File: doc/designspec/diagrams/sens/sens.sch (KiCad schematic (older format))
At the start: 7 parts

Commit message: sensormodul schema, spi, led display, filters är på g
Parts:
- removed U?: ATmega1284-PU, Package_DIP:DIP-40_W15.24mm, symbol _NONAME_
- added U?: ADG419BN, Package_DIP:DIP-8_W7.62mm, symbol Analog_Switch:ADG419BN
- added _?: JMA162A, Display_7Segment:DA04-11SYKWA, symbol jma162a:JMA162A
- HALLEFFECTSENSOR: symbol hall-effect:A112X -> sens-rescue:A112X-hall-effect
- KRISTALLOSCILLATOR: symbol exo3:IQEXO-3 -> sens-rescue:IQEXO-3-exo3
- U?: symbol MCU_Microchip_ATmega:ATmega1284-PU -> sens-rescue:ATmega1284-PU-MCU_Microchip_ATmega
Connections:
- net labels added: MISO, MOSI, SPI_SCK, SS_Slave_Select
- wire segments 39 -> 76
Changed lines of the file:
@@
 $EndComp
-Wire Wire Line
-	6200 4350 8850 4350
 Wire Wire Line
 	8600 1450 6200 1450
@@
 Wire Wire Line
 	8250 1650 6200 1650
-Wire Wire Line
-	8200 5850 8200 4500
-Wire Wire Line
-	8200 4500 8850 4500
-Connection ~ 8200 4500
 Wire Wire Line
 	8200 2650 8800 2650
@@
 Connection ~ 8450 2050
 Wire Wire Line
-	8450 4650 8850 4650
-Wire Wire Line
 	5700 1050 5700 1150
 Wire Wire Line
@@
 Wire Wire Line
 	6600 3750 6200 3750
-Wire Wire Line
-	7200 2950 7200 1050
 Connection ~ 7200 1050
 Wire Wire Line
@@
 Wire Wire Line
 	7100 4150 7100 5850
-Connection ~ 7100 5850
-Wire Wire Line
-	7100 5850 8200 5850
-$Comp
-L _NONAME_ U?
-U 1 1 5BC75C71
-P 0 0
-F 0 "U?" H 5600 1064 50  0000 C CNN
-F 1 "ATmega1284-PU" H 5600 973 50  0000 C CNN
-F 2 "Package_DIP:DIP-40_W15.24mm" H 5600 3150 50  0001 C CIN
-F 3 "http://ww1.microchip.com/downloads/en/DeviceDoc/Atmel-8272-8-bit-AVR-microcontroller-ATmega164A_PA-324A_PA-644A_PA-1284_P_datasheet.pdf" H 5600 3150 50  0001 C CNN
-	1    0    0
-	1    0    0    -1
-$EndComp
-$Comp
-L exo3:IQEXO-3 KRISTALLOSCILLATOR
+$Comp
+L sens-rescue:IQEXO-3-exo3 KRISTALLOSCILLATOR
 U 1 1 5BDCCBF2
-P 3150 2400
-F 0 "KRISTALLOSCILLATOR" V 3196 2070 50  0000 R CNN
-F 1 "IQEXO-3" V 3105 2070 50  0000 R CNN
-F 2 "Package_SO:SOIC-8_3.9x4.9mm_P1.27mm" H 3200 1650 50  0001 C CNN
-F 3 "http://www.onsemi.com/pub/Collateral/NB3N511-D.PDF" H 3200 1550 50  0001 C CNN
-	1    3150 2400
-	0    -1   -1   0
-$EndComp
-Wire Wire Line
-	5600 5850 3350 5850
-Wire Wire Line
-	3350 5850 3350 2800
-Wire Wire Line
-	2850 2000 2850 1050
-Wire Wire Line
-	2850 1050 5600 1050
+P 3550 2400
+F 0 "KRISTALLOSCILLATOR" V 3596 2070 50  0000 R CNN
+F 1 "IQEXO-3" V 3505 2070 50  0000 R CNN
+F 2 "Package_SO:SOIC-8_3.9x4.9mm_P1.27mm" H 3600 1650 50  0001 C CNN
+F 3 "http://www.onsemi.com/pub/Collateral/NB3N511-D.PDF" H 3600 1550 50  0001 C CNN
+	1    3550 2400
+	0    1    -1   0
+$EndComp
+Wire Wire Line
+	3850 2000 3850 1050
 Connection ~ 5600 1050
 $Comp
-L MCU_Microchip_ATmega:ATmega1284-PU U?
+L sens-rescue:ATmega1284-PU-MCU_Microchip_ATmega U?
 U 1 1 5BDC5F4E
 P 5600 3150
@@
 	1    0    0    -1
 $EndComp
+$Comp
+L sens-rescue:ACS715xLCTR-30A-taxi-sens-rescue AVSTÅNDSMÄTARE(SIDA)
+U 1 1 5BDC9DEC
+P 8900 1450
+F 0 "AVSTÅNDSMÄTARE(SIDA)" H 8250 1550 50  0000 C CNN
+F 1 "GP2D120" H 8300 1450 50  0000 C CNN
+F 2 "Package_SO:SOIC-8_3.9x4.9mm_P1.27mm" H 9000 1100 50  0001 L CIN
+F 3 "http://www.allegromicro.com/~/media/Files/Datasheets/ACS715-Datasheet.ashx?la=en" H 8900 1450 50  0001 C CNN
+	1    8900 1450
+	-1   0    0    -1
+$EndComp
+$Comp
+L power:+5V #PWR?
+U 1 1 5BDC9F18
+P 7000 800
+F 0 "#PWR?" H 7000 650 50  0001 C CNN
+F 1 "+5V" H 7015 973 50  0000 C CNN
+F 2 "" H 7000 800 50  0001 C CNN
+F 3 "" H 7000 800 50  0001 C CNN
+	1    7000 800
+	1    0    0    -1
+$EndComp
+$Comp
+L sens-rescue:A112X-hall-effect HALLEFFECTSENSOR
+U 1 1 5BDCB7F9
+P 8900 3650
+F 0 "HALLEFFECTSENSOR" H 9129 3696 50  0000 L CNN
+F 1 "A112X" H 9129 3605 50  0000 L CNN
+F 2 "Package_TO_SOT_SMD:SOT-23" H 8900 3300 50  0001 L CIN
+F 3 "http://www.allegromicro.com/en/Products/Part_Numbers/1101/1101.pdf" H 8900 4300 50  0001 C CNN
+	1    8900 3650
+	1    0    0    -1
+$EndComp
+$Comp
+L power:GNDREF #PWR?
+U 1 1 5BDCBACA
+P 5600 5850
+F 0 "#PWR?" H 5600 5600 50  0001 C CNN
+F 1 "GNDREF" H 5605 5677 50  0000 C CNN
+F 2 "" H 5600 5850 50  0001 C CNN
+F 3 "" H 5600 5850 50  0001 C CNN
+	1    5600 5850
+	1    0    0    -1
+$EndComp
+Wire Wire Line
+	3850 1050 5600 1050
+Wire Wire Line
+	3850 2800 4200 2800
+Wire Wire Line
+	4200 2800 4200 1650
+Wire Wire Line
+	4200 1650 5000 1650
+$Comp
+L jma162a:JMA162A _?
+U 1 1 5BDF0219
+P 8100 5100
+F 0 "_?" H 8100 5050 50  0001 C CNN
+F 1 "JMA162A" H 8100 4525 50  0000 C CNN
+F 2 "Display_7Segment:DA04-11SYKWA" V 9275 5075 50  0001 C CNN
+F 3 "http://www.kingbright.com/attachments/file/psearch/000/00/00/DA04-11SYKWA(Ver.6A).pdf" H 7980 4700 50  0001 C CNN
+	1    8100 5100
+	-1   0    0    -1
+$EndComp
+$Comp
+L power:GNDREF #PWR?
+U 1 1 5BDF121A
+P 3350 2800
+F 0 "#PWR?" H 3350 2550 50  0001 C CNN
+F 1 "GNDREF" H 3355 2627 50  0000 C CNN
+F 2 "" H 3350 2800 50  0001 C CNN
+F 3 "" H 3350 2800 50  0001 C CNN
+	1    3350 2800
+	1    0    0    -1
+$EndComp
+$Comp
+L power:GNDREF #PWR?
+U 1 1 5BDF1A61
+P 8800 5450
+F 0 "#PWR?" H 8800 5200 50  0001 C CNN
+F 1 "GNDREF" H 8805 5277 50  0000 C CNN
+F 2 "" H 8800 5450 50  0001 C CNN
+F 3 "" H 8800 5450 50  0001 C CNN
+	1    8800 5450
+	0    -1   -1   0
+$EndComp
+Connection ~ 3850 1050
+Wire Wire Line
+	3850 1050 2050 1050
+Text Label 6200 2750 0    50   ~ 0
+SS_Slave_Select
+Text Label 6200 2850 0    50   ~ 0
+MOSI
+Text Label 6200 2950 0    50   ~ 0
+MISO
+Text Label 6200 3050 0    50   ~ 0
+SPI_SCK
 $Comp
 L Connector:AVR-JTAG-10 J?
@@
 $EndComp
 Wire Wire Line
-	8450 2050 8450 4650
-Wire Wire Line
-	8200 2650 8200 4500
-$Comp
-L sens-rescue:ACS715xLCTR-30A-taxi-sens-rescue AVSTÅNDSMÄTARE(SIDA)
-U 1 1 5BDC9DEC
-P 8900 1450
-F 0 "AVSTÅNDSMÄTARE(SIDA)" H 8250 1550 50  0000 C CNN
-F 1 "GP2D120" H 8300 1450 50  0000 C CNN
-F 2 "Package_SO:SOIC-8_3.9x4.9mm_P1.27mm" H 9000 1100 50  0001 L CIN
-F 3 "http://www.allegromicro.com/~/media/Files/Datasheets/ACS715-Datasheet.ashx?la=en" H 8900 1450 50  0001 C CNN
-	1    8900 1450
-	-1   0    0    -1
-$EndComp
-$Comp
-L power:+5V #PWR?
-U 1 1 5BDC9F18
-P 7000 800
-F 0 "#PWR?" H 7000 650 50  0001 C CNN
-F 1 "+5V" H 7015 973 50  0000 C CNN
-F 2 "" H 7000 800 50  0001 C CNN
-F 3 "" H 7000 800 50  0001 C CNN
-	1    7000 800
-	1    0    0    -1
-$EndComp
-$Comp
-L hall-effect:A112X HALLEFFECTSENSOR
-U 1 1 5BDCB7F9
-P 9150 4500
-F 0 "HALLEFFECTSENSOR" H 9379 4546 50  0000 L CNN
-F 1 "A112X" H 9379 4455 50  0000 L CNN
-F 2 "Package_TO_SOT_SMD:SOT-23" H 9150 4150 50  0001 L CIN
-F 3 "http://www.allegromicro.com/en/Products/Part_Numbers/1101/1101.pdf" H 9150 5150 50  0001 C CNN
-	1    9150 4500
-	1    0    0    -1
-$EndComp
-$Comp
-L power:GNDREF #PWR?
-U 1 1 5BDCBACA
-P 5600 5850
-F 0 "#PWR?" H 5600 5600 50  0001 C CNN
-F 1 "GNDREF" H 5605 5677 50  0000 C CNN
-F 2 "" H 5600 5850 50  0001 C CNN
-F 3 "" H 5600 5850 50  0001 C CNN
-	1    5600 5850
-	1    0    0    -1
-$EndComp
+	7200 2950 7200 1050
+Wire Wire Line
+	6200 2750 6850 2750
+Wire Wire Line
+	6200 2850 6850 2850
+Wire Wire Line
+	6200 2950 6850 2950
+Wire Wire Line
+	6200 3050 6850 3050
+Wire Wire Line
+	8200 2650 8200 3650
+Wire Wire Line
+	8450 2050 8450 3800
+Wire Wire Line
+	8600 3800 8450 3800
+Wire Wire Line
+	8600 3650 8200 3650
+Wire Wire Line
+	7100 5850 9100 5850
+Wire Wire Line
+	9100 5850 9100 4000
+Wire Wire Line
+	9100 4000 8200 4000
+Wire Wire Line
+	8200 4000 8200 3650
+Connection ~ 7100 5850
+Connection ~ 8200 3650
+Wire Wire Line
+	8350 4550 8350 4500
+Wire Wire Line
+	8350 3800 8450 3800
+Connection ~ 8350 4500
+Wire Wire Line
+	8350 4500 8350 3800
+Connection ~ 8450 3800
+Wire Wire Line
+	7400 4650 7400 4150
+Wire Wire Line
+	6200 4150 7400 4150
+Wire Wire Line
+	7400 4750 7250 4750
+Wire Wire Line
+	7250 4750 7250 4250
+Wire Wire Line
+	7250 4250 6200 4250
+Wire Wire Line
+	7400 4850 7150 4850
+Wire Wire Line
+	7150 4850 7150 4350
+Wire Wire Line
+	6200 4350 7150 4350
+Wire Wire Line
+	7400 4950 7050 4950
+Wire Wire Line
+	7050 4950 7050 4450
+Wire Wire Line
+	7050 4450 6200 4450
+Wire Wire Line
+	7400 5050 6950 5050
+Wire Wire Line
+	6950 5050 6950 4550
+Wire Wire Line
+	6950 4550 6200 4550
+Wire Wire Line
+	6200 4650 6900 4650
+Wire Wire Line
+	6900 4650 6900 5150
+Wire Wire Line
+	6900 5150 7400 5150
+Wire Wire Line
+	7400 5250 6800 5250
+Wire Wire Line
+	6800 5250 6800 4750
+Wire Wire Line
+	6800 4750 6200 4750
+Wire Wire Line
+	6200 4850 6700 4850
+Wire Wire Line
+	6700 4850 6700 5350
+Wire Wire Line
+	6700 5350 7400 5350
+Wire Wire Line
+	7400 5450 6500 5450
+Wire Wire Line
+	6500 5450 6500 3950
+Wire Wire Line
+	6500 3950 6200 3950
+$Comp
+L Analog_Switch:ADG419BN U?
+U 1 1 5BE987B7
+P 2650 1450
+F 0 "U?" H 2650 1692 50  0000 C CNN
+F 1 "ADG419BN" H 2650 1601 50  0000 C CNN
+F 2 "Package_DIP:DIP-8_W7.62mm" H 2650 1150 50  0001 C CNN
+F 3 "http://www.analog.com/media/en/technical-documentation/data-sheets/ADG419.pdf" H 2650 1250 50  0001 C CNN
+	1    2650 1450
+	1    0    0    -1
+$EndComp
+Wire Wire Line
+	2950 1450 5000 1450
 $EndSCHEMATC

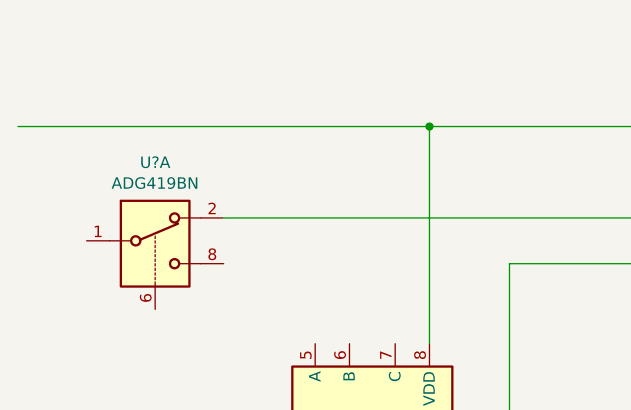
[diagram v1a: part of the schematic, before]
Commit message: Schematics done, need filters for sensors, some resistors for the switches etc
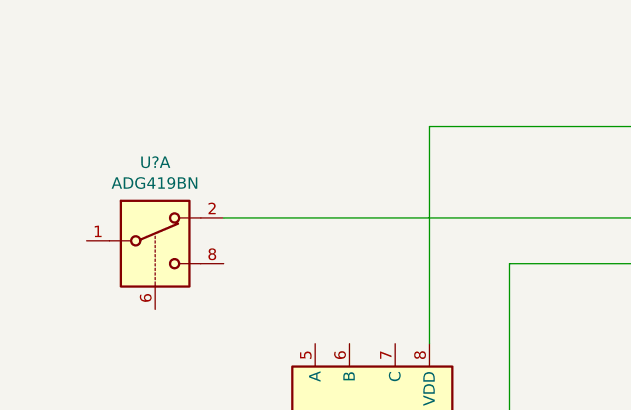
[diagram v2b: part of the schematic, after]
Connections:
- wire segments 76 -> 75
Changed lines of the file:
@@
 	0    -1   -1   0
 $EndComp
-Connection ~ 3850 1050
-Wire Wire Line
-	3850 1050 2050 1050
 Text Label 6200 2750 0    50   ~ 0
 SS_Slave_Select

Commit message: final stage of schematics first assignment
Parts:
- removed HALLEFFECTSENSOR: A112X, Package_TO_SOT_SMD:SOT-23, symbol sens-rescue:A112X-hall-effect
- added C?: 100nF, symbol pspice:CAP
- added HALLEFFECTSENSOR? (x2): A112X, Package_TO_SOT_SMD:SOT-23, symbol sens-rescue:A112X-hall-effect
- added L?: 10uH, symbol pspice:INDUCTOR
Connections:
- wire segments 75 -> 64
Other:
- moved on the sheet: J?

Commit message: Updated reset switch for reset and styr
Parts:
- removed U?: ADG419BN, Package_DIP:DIP-8_W7.62mm, symbol Analog_Switch:ADG419BN
- added C?: 100nF, symbol pspice:CAP
- added R?: R, symbol pspice:R
- added U?: Tryckkknapp, Package_DIP:DIP-8_W7.62mm, symbol Analog_Switch:ADG417BN
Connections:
- wire segments 64 -> 70
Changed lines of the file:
@@
 Wire Wire Line
 	6500 3950 6200 3950
-$Comp
-L Analog_Switch:ADG419BN U?
-U 1 1 5BE987B7
-P 2650 1450
-F 0 "U?" H 2650 1692 50  0000 C CNN
-F 1 "ADG419BN" H 2650 1601 50  0000 C CNN
-F 2 "Package_DIP:DIP-8_W7.62mm" H 2650 1150 50  0001 C CNN
-F 3 "http://www.analog.com/media/en/technical-documentation/data-sheets/ADG419.pdf" H 2650 1250 50  0001 C CNN
-	1    2650 1450
-	1    0    0    -1
-$EndComp
-Wire Wire Line
-	2950 1450 5000 1450
 Wire Wire Line
 	8250 1650 6200 1650
@@
 	0    -1   -1   0
 $EndComp
+$Comp
+L Analog_Switch:ADG417BN U?
+U 1 1 5BE1E411
+P 3550 1200
+F 0 "U?" H 3550 1467 50  0000 C CNN
+F 1 "Tryckkknapp" H 3550 1376 50  0000 C CNN
+F 2 "Package_DIP:DIP-8_W7.62mm" H 3550 1100 50  0001 C CNN
+F 3 "http://www.analog.com/media/en/technical-documentation/data-sheets/ADG417.pdf" H 3550 1200 50  0001 C CNN
+	1    3550 1200
+	1    0    0    -1
+$EndComp
+$Comp
+L pspice:R R?
+U 1 1 5BE20DAD
+P 3550 800
+F 0 "R?" V 3345 800 50  0000 C CNN
+F 1 "R" V 3436 800 50  0000 C CNN
+F 2 "" H 3550 800 50  0001 C CNN
+F 3 "" H 3550 800 50  0001 C CNN
+	1    3550 800
+	0    1    1    0
+$EndComp
+$Comp
+L pspice:CAP C?
+U 1 1 5BE20E58
+P 3550 1750
+F 0 "C?" V 3235 1750 50  0000 C CNN
+F 1 "100nF" V 3326 1750 50  0000 C CNN
+F 2 "" H 3550 1750 50  0001 C CNN
+F 3 "" H 3550 1750 50  0001 C CNN
+	1    3550 1750
+	0    1    1    0
+$EndComp
+$Comp
+L power:GNDREF #PWR?
+U 1 1 5BE27324
+P 3300 1750
+F 0 "#PWR?" H 3300 1500 50  0001 C CNN
+F 1 "GNDREF" H 3305 1577 50  0000 C CNN
+F 2 "" H 3300 1750 50  0001 C CNN
+F 3 "" H 3300 1750 50  0001 C CNN
+	1    3300 1750
+	1    0    0    -1
+$EndComp
+$Comp
+L power:GNDREF #PWR?
+U 1 1 5BE29C00
+P 3250 1200
+F 0 "#PWR?" H 3250 950 50  0001 C CNN
+F 1 "GNDREF" H 3255 1027 50  0000 C CNN
+F 2 "" H 3250 1200 50  0001 C CNN
+F 3 "" H 3250 1200 50  0001 C CNN
+	1    3250 1200
+	1    0    0    -1
+$EndComp
+Wire Wire Line
+	3800 800  3850 800
+Wire Wire Line
+	3850 800  3850 1200
+Wire Wire Line
+	3800 1750 3850 1750
+Wire Wire Line
+	3850 1750 3850 1200
+Connection ~ 3850 1200
+Wire Wire Line
+	5000 1450 4200 1450
+Wire Wire Line
+	4200 1450 4200 1200
+Wire Wire Line
+	4200 1200 3850 1200
+$Comp
+L power:+5V #PWR?
+U 1 1 5BE2E277
+P 3300 800
+F 0 "#PWR?" H 3300 650 50  0001 C CNN
+F 1 "+5V" V 3315 928 50  0000 L CNN
+F 2 "" H 3300 800 50  0001 C CNN
+F 3 "" H 3300 800 50  0001 C CNN
+	1    3300 800
+	0    -1   -1   0
+$EndComp

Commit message: Added LP-filters between sensors
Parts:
- removed C?: 100nF, symbol pspice:CAP
- removed L?: 10uH, symbol pspice:INDUCTOR
- added 100nF (x2), C?: CAP, symbol pspice:CAP
- added 18kohm (x2): R, symbol pspice:R
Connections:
- wire segments 70 -> 61
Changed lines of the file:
@@
 $EndDescr
-Wire Wire Line
-	8600 2350 8250 2350
-Wire Wire Line
-	8250 2350 8250 1650
 Wire Wire Line
 	5600 5150 5600 5850
@@
 	6200 3050 6850 3050
 Wire Wire Line
-	8350 4550 8350 4500
-Wire Wire Line
 	7400 4750 7250 4750
 Wire Wire Line
@@
 	7050 4450 6200 4450
 Wire Wire Line
-	7400 5050 6950 5050
-Wire Wire Line
-	6950 5050 6950 4550
-Wire Wire Line
-	6950 4550 6200 4550
-Wire Wire Line
-	6200 4650 6900 4650
-Wire Wire Line
-	6900 4650 6900 5150
-Wire Wire Line
-	6900 5150 7400 5150
-Wire Wire Line
-	7400 5250 6800 5250
-Wire Wire Line
-	6800 5250 6800 4750
-Wire Wire Line
-	6800 4750 6200 4750
-Wire Wire Line
-	6200 4850 6700 4850
-Wire Wire Line
-	6700 4850 6700 5350
-Wire Wire Line
-	6700 5350 7400 5350
-Wire Wire Line
 	7400 5450 6500 5450
 Wire Wire Line
@@
 Wire Wire Line
 	6500 3950 6200 3950
-Wire Wire Line
-	8250 1650 6200 1650
-Wire Wire Line
-	8600 1450 6200 1450
 $Comp
 L power:+5V #PWR?
@@
 $EndComp
 $Comp
-L pspice:CAP C?
-U 1 1 5BE52B56
-P 6600 950
-F 0 "C?" V 6285 950 50  0000 C CNN
-F 1 "100nF" V 6376 950 50  0000 C CNN
-F 2 "" H 6600 950 50  0001 C CNN
-F 3 "" H 6600 950 50  0001 C CNN
-	1    6600 950
-	0    1    1    0
-$EndComp
-$Comp
-L pspice:INDUCTOR L?
-U 1 1 5BE52C21
-P 5750 950
-F 0 "L?" H 5750 1165 50  0000 C CNN
-F 1 "10uH" H 5750 1074 50  0000 C CNN
-F 2 "" H 5750 950 50  0001 C CNN
-F 3 "" H 5750 950 50  0001 C CNN
-	1    5750 950
-	1    0    0    -1
-$EndComp
-Wire Wire Line
-	6000 950  6200 950
-Wire Wire Line
-	5700 1150 6200 1150
-Wire Wire Line
-	6200 1150 6200 950
-Connection ~ 6200 950
-Wire Wire Line
-	6200 950  6350 950
-Wire Wire Line
-	5500 950  5500 1050
-Wire Wire Line
-	5500 1050 5600 1050
-Wire Wire Line
-	5600 1050 5600 1150
-$Comp
-L power:GNDREF #PWR?
-U 1 1 5BE56585
-P 6850 950
-F 0 "#PWR?" H 6850 700 50  0001 C CNN
-F 1 "GNDREF" V 6855 822 50  0000 R CNN
-F 2 "" H 6850 950 50  0001 C CNN
-F 3 "" H 6850 950 50  0001 C CNN
-	1    6850 950
-	0    -1   -1   0
-$EndComp
-$Comp
 L Analog_Switch:ADG417BN U?
 U 1 1 5BE1E411
@@
 	0    -1   -1   0
 $EndComp
+$Comp
+L power:+5V #PWR?
+U 1 1 5BE4E70D
+P 8350 4500
+F 0 "#PWR?" H 8350 4350 50  0001 C CNN
+F 1 "+5V" H 8365 4673 50  0000 C CNN
+F 2 "" H 8350 4500 50  0001 C CNN
+F 3 "" H 8350 4500 50  0001 C CNN
+	1    8350 4500
+	1    0    0    -1
+$EndComp
+$Comp
+L pspice:CAP 100nF
+U 1 1 5BE568F2
+P 7600 2100
+F 0 "100nF" H 7422 2146 50  0000 R CNN
+F 1 "CAP" H 7422 2055 50  0000 R CNN
+F 2 "" H 7600 2100 50  0001 C CNN
+F 3 "" H 7600 2100 50  0001 C CNN
+	1    7600 2100
+	-1   0    0    -1
+$EndComp
+$Comp
+L pspice:CAP 100nF
+U 1 1 5BE569D7
+P 7850 1300
+F 0 "100nF" H 7672 1346 50  0000 R CNN
+F 1 "CAP" H 7672 1255 50  0000 R CNN
+F 2 "" H 7850 1300 50  0001 C CNN
+F 3 "" H 7850 1300 50  0001 C CNN
+	1    7850 1300
+	-1   0    0    -1
+$EndComp
+$Comp
+L pspice:R 18kohm
+U 1 1 5BE56A96
+P 8100 1050
+F 0 "18kohm" V 8305 1050 50  0000 C CNN
+F 1 "R" V 8214 1050 50  0000 C CNN
+F 2 "" H 8100 1050 50  0001 C CNN
+F 3 "" H 8100 1050 50  0001 C CNN
+	1    8100 1050
+	0    1    -1   0
+$EndComp
+$Comp
+L pspice:R 18kohm
+U 1 1 5BE56AF9
+P 7850 1850
+F 0 "18kohm" V 8055 1850 50  0000 C CNN
+F 1 "R" V 7964 1850 50  0000 C CNN
+F 2 "" H 7850 1850 50  0001 C CNN
+F 3 "" H 7850 1850 50  0001 C CNN
+	1    7850 1850
+	0    1    -1   0
+$EndComp
+Wire Wire Line
+	8600 1450 8350 1450
+Wire Wire Line
+	8350 1450 8350 1050
+Wire Wire Line
+	8600 2350 8600 1850
+Wire Wire Line
+	8600 1850 8100 1850
+Wire Wire Line
+	7600 1850 6850 1850
+Connection ~ 7600 1850
+$Comp
+L power:GNDREF #PWR?
+U 1 1 5BE81361
+P 7600 2350
+F 0 "#PWR?" H 7600 2100 50  0001 C CNN
+F 1 "GNDREF" V 7605 2222 50  0000 R CNN
+F 2 "" H 7600 2350 50  0001 C CNN
+F 3 "" H 7600 2350 50  0001 C CNN
+	1    7600 2350
+	0    -1   -1   0
+$EndComp
+$Comp
+L power:GNDREF #PWR?
+U 1 1 5BE82602
+P 7850 1550
+F 0 "#PWR?" H 7850 1300 50  0001 C CNN
+F 1 "GNDREF" V 7855 1422 50  0000 R CNN
+F 2 "" H 7850 1550 50  0001 C CNN
+F 3 "" H 7850 1550 50  0001 C CNN
+	1    7850 1550
+	0    -1   -1   0
+$EndComp
+Wire Wire Line
+	7850 1050 7400 1050
+Wire Wire Line
+	7400 1050 7400 1450
+Wire Wire Line
+	6200 1450 7400 1450
+Connection ~ 7850 1050
+Wire Wire Line
+	6200 1550 6850 1550
+Wire Wire Line
+	6850 1550 6850 1850
+$Comp
+L pspice:CAP C?
+U 1 1 5BEA46CC
+P 5650 800
+F 0 "C?" V 5335 800 50  0000 C CNN
+F 1 "CAP" V 5426 800 50  0000 C CNN
+F 2 "" H 5650 800 50  0001 C CNN
+F 3 "" H 5650 800 50  0001 C CNN
+	1    5650 800
+	0    1    1    0
+$EndComp
+$Comp
+L power:GNDREF #PWR?
+U 1 1 5BEA491F
+P 5400 800
+F 0 "#PWR?" H 5400 550 50  0001 C CNN
+F 1 "GNDREF" V 5405 672 50  0000 R CNN
+F 2 "" H 5400 800 50  0001 C CNN
+F 3 "" H 5400 800 50  0001 C CNN
+	1    5400 800
+	0    1    1    0
+$EndComp
+Wire Wire Line
+	5700 1150 5900 1150
+Wire Wire Line
+	5900 1150 5900 1050
+Wire Wire Line
+	5600 1150 5600 1050
+Wire Wire Line
+	5600 1050 5900 1050
+Connection ~ 5900 1050
+Wire Wire Line
+	5900 1050 5900 800
 $EndSCHEMATC
